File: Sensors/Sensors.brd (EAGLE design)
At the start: 101.6 x 53.3 mm, 36 parts, among them J2 JST_CONNECTOR, J6 JST_CONNECTOR, J7 JST_CONNECTOR, J8 JST_CONNECTOR, J9 JST_CONNECTOR

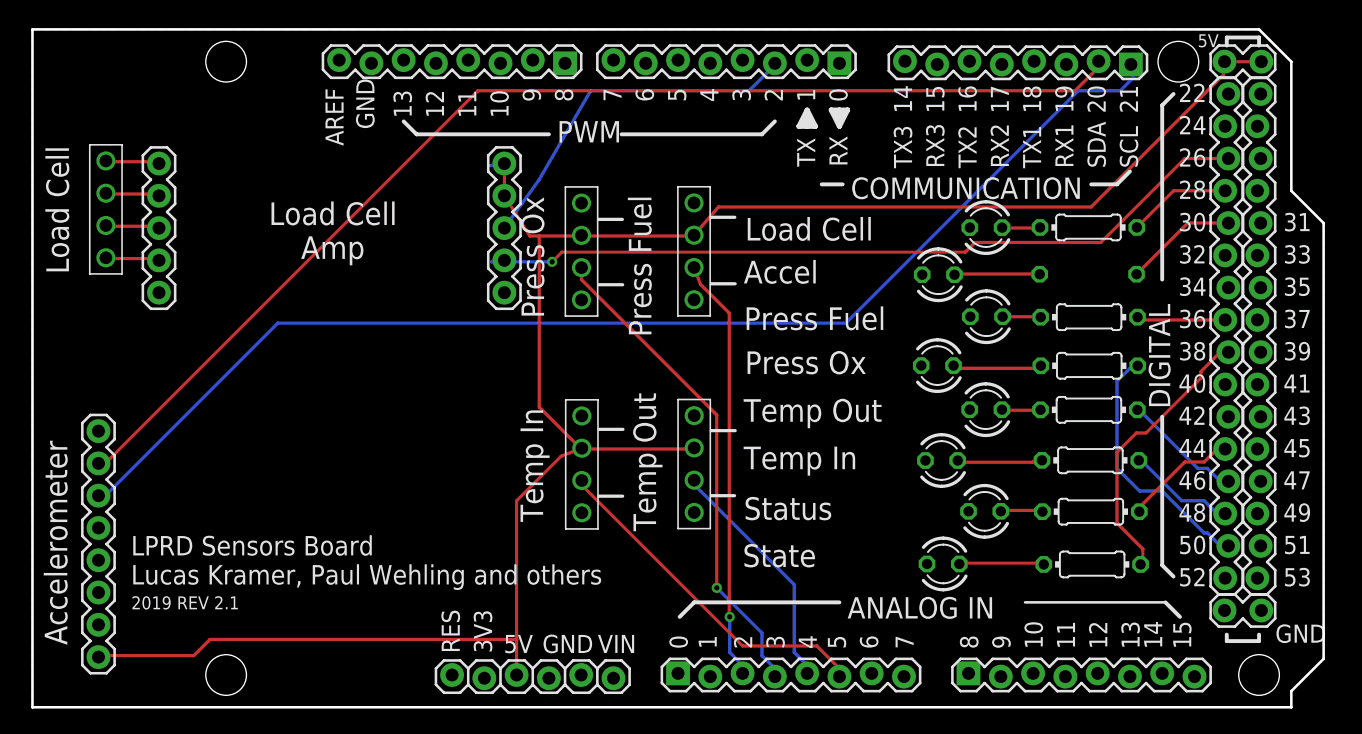
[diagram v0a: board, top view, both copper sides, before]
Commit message: Fix misc. problems found by DRC
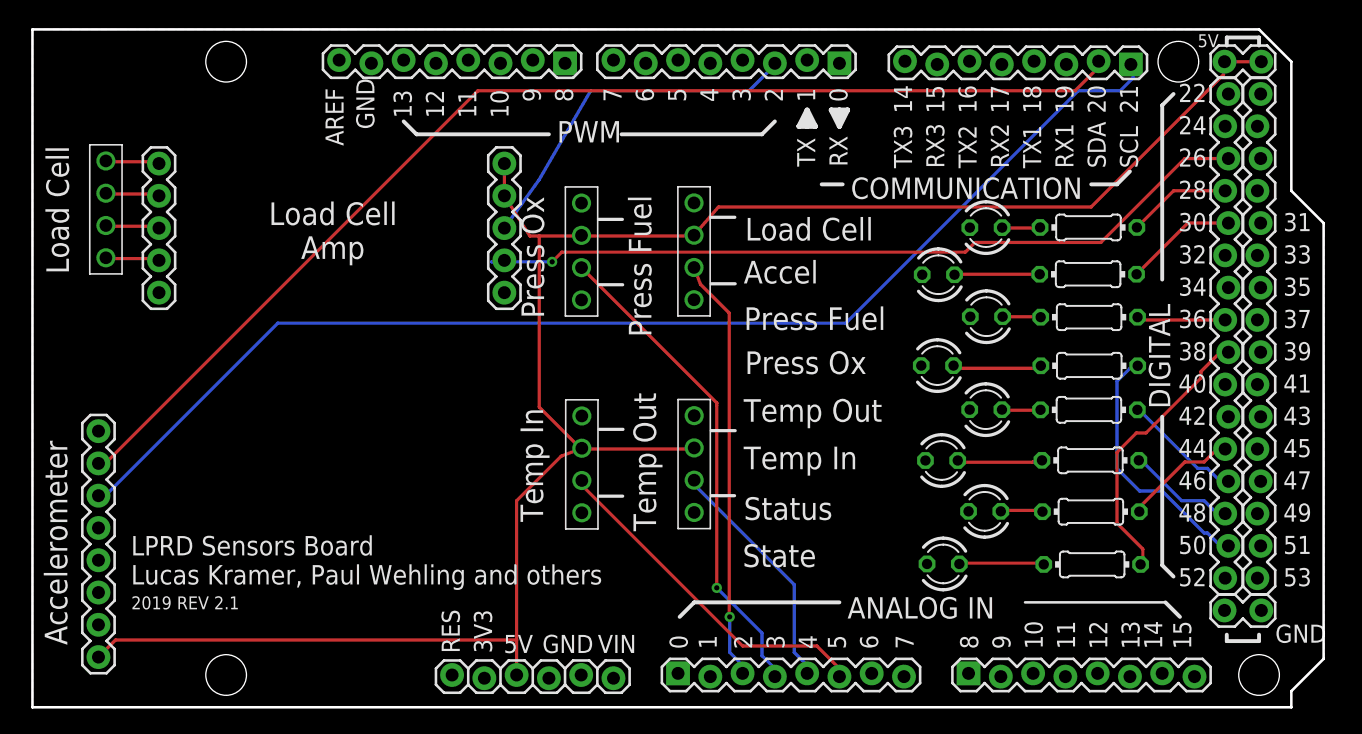
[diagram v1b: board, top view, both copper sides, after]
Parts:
- flipped R1 to the top, turned to 180 degrees
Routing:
- net 5V: track 152.9 -> 151.7 mm
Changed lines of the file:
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@@
 <element name="J9" library="LPRD_RELAY" library_urn="urn:adsk.eagle:library:14231923" package="B4B-XH-A(LF)(SN)" package3d_urn="urn:adsk.eagle:package:14231943/1" value="JST_CONNECTOR" x="43.2054" y="37.1348" smashed="yes" rot="R90"/>
 <element name="J2" library="LPRD_RELAY" library_urn="urn:adsk.eagle:library:14231923" package="B4B-XH-A(LF)(SN)" package3d_urn="urn:adsk.eagle:package:14231943/1" value="JST_CONNECTOR" x="5.7785" y="40.4495" smashed="yes" rot="R90"/>
-<element name="R1" library="rcl" library_urn="urn:adsk.eagle:library:334" package="0204/7" package3d_urn="urn:adsk.eagle:package:23498/2" value="1000" x="83.0707" y="34.0741" smashed="yes" rot="MR0">
-<attribute name="POPULARITY" value="48" x="83.0707" y="34.0741" size="1.778" layer="28" rot="MR0" display="off"/>
-<attribute name="SPICEPREFIX" value="R" x="83.0707" y="34.0741" size="1.778" layer="28" rot="MR0" display="off"/>
+<element name="R1" library="rcl" library_urn="urn:adsk.eagle:library:334" package="0204/7" package3d_urn="urn:adsk.eagle:package:23498/2" value="1000" x="83.0707" y="34.0741" smashed="yes" rot="R180">
+<attribute name="POPULARITY" value="48" x="83.0707" y="34.0741" size="1.778" layer="27" rot="R180" display="off"/>
+<attribute name="SPICEPREFIX" value="R" x="83.0707" y="34.0741" size="1.778" layer="27" rot="R180" display="off"/>
 </element>
 <element name="LED1" library="led" library_urn="urn:adsk.eagle:library:259" package="LED3MM" package3d_urn="urn:adsk.eagle:package:15797/1" value="" x="71.2851" y="34.036" smashed="yes" rot="R180">
@@
 <wire x1="43.3197" y1="20.32" x2="43.2308" y2="20.3835" width="0.254" layer="1"/>
 <wire x1="51.9684" y1="20.32" x2="52.07" y2="20.4089" width="0.254" layer="1"/>
-<wire x1="5.26415" y1="4.00685" x2="5.1943" y2="3.9497" width="0.254" layer="1"/>
 <wire x1="43.0657" y1="37.084" x2="43.2054" y2="37.1348" width="0.254" layer="1"/>
-<wire x1="36.0172" y1="42.6212" x2="37.1348" y2="42.7863" width="0.254" layer="16"/>
 <wire x1="43.0657" y1="37.084" x2="39.878" y2="37.084" width="0.254" layer="1"/>
 <wire x1="39.878" y1="37.084" x2="39.1414" y2="37.084" width="0.254" layer="1"/>
 <wire x1="39.1414" y1="37.084" x2="37.1348" y2="40.2463" width="0.254" layer="1"/>
 <wire x1="37.1348" y1="40.2463" x2="37.1348" y2="42.7863" width="0.254" layer="1"/>
-<wire x1="38.1" y1="16.256" x2="38.1" y2="5.334" width="0.254" layer="1"/>
-<wire x1="38.1" y1="5.334" x2="38.1" y2="2.54" width="0.254" layer="1"/>
+<wire x1="38.1" y1="16.256" x2="38.1" y2="5.2959" width="0.254" layer="1"/>
+<wire x1="38.1" y1="5.2959" x2="38.1" y2="2.54" width="0.254" layer="1"/>
 <wire x1="41.6004375" y1="19.7564375" x2="38.1" y2="16.256" width="0.254" layer="1"/>
 <wire x1="41.6004375" y1="19.7564375" x2="43.2308" y2="20.3835" width="0.254" layer="1"/>
-<wire x1="12.7" y1="4.064" x2="5.334" y2="4.064" width="0.254" layer="1"/>
-<wire x1="13.97" y1="5.334" x2="12.7" y2="4.064" width="0.254" layer="1"/>
-<wire x1="38.1" y1="5.334" x2="13.97" y2="5.334" width="0.254" layer="1"/>
-<wire x1="5.334" y1="4.064" x2="5.1943" y2="3.9497" width="0.254" layer="1"/>
 <wire x1="43.2816" y1="20.2184" x2="43.4213" y2="20.2184" width="0.254" layer="1"/>
 <wire x1="39.878" y1="23.622" x2="43.2816" y2="20.2184" width="0.254" layer="1"/>
 <wire x1="39.878" y1="37.084" x2="39.878" y2="23.622" width="0.254" layer="1"/>
 <wire x1="43.4213" y1="20.2184" x2="43.2308" y2="20.3835" width="0.254" layer="1"/>
+<wire x1="5.1943" y1="3.9497" x2="6.5405" y2="5.2959" width="0.254" layer="1"/>
+<wire x1="6.5405" y1="5.2959" x2="38.1" y2="5.2959" width="0.254" layer="1"/>
 </signal>
 <signal name="GND">
@@
 <contactref element="LED8" pad="K"/>
 <contactref element="LED10" pad="K"/>
-<wire x1="26.67" y1="50.5206" x2="26.67" y2="50.673" width="0.254" layer="16"/>
 <contactref element="J6" pad="P$4"/>
 <contactref element="J7" pad="P$4"/>
@@
 <contactref element="JP7" pad="4"/>
 <contactref element="J9" pad="P$2"/>
-<wire x1="43.2054" y1="34.5948" x2="43.2054" y2="33.6423" width="0.254" layer="1"/>
-<wire x1="53.848" y1="22.9997" x2="43.2054" y2="33.6423" width="0.254" layer="1"/>
-<wire x1="53.848" y1="9.398" x2="53.848" y2="22.9997" width="0.254" layer="1"/>
+<wire x1="53.848" y1="9.398" x2="53.848" y2="23.749" width="0.254" layer="1"/>
+<wire x1="53.848" y1="23.749" x2="53.848" y2="23.9395" width="0.254" layer="1"/>
 <wire x1="57.404" y1="5.842" x2="53.848" y2="9.398" width="0.254" layer="16"/>
 <wire x1="57.404" y1="4.064" x2="57.404" y2="5.842" width="0.254" layer="16"/>
@@
 <wire x1="58.42" y1="2.413" x2="58.42" y2="3.048" width="0.254" layer="16"/>
 <via x="53.848" y="9.398" extent="1-16" drill="0.4064"/>
+<wire x1="43.2054" y1="34.5948" x2="53.848" y2="23.9522" width="0.254" layer="1"/>
+<wire x1="53.848" y1="23.9522" x2="53.848" y2="23.9395" width="0.254" layer="1"/>
 </signal>
 <signal name="VOUT_PRESSURE_OX">
@@
 <contactref element="JP9" pad="12"/>
 <contactref element="R1" pad="1"/>
-<wire x1="94.107" y1="38.1" x2="90.9066" y2="38.1" width="0.254" layer="1"/>
-<wire x1="90.9066" y1="38.1" x2="86.8807" y2="34.0741" width="0.254" layer="1"/>
+<wire x1="86.8807" y1="34.0741" x2="90.9066" y2="38.1" width="0.254" layer="1"/>
+<wire x1="90.9066" y1="38.1" x2="94.107" y2="38.1" width="0.254" layer="1"/>
 </signal>
 <signal name="STATE_LED">
@@
 <contactref element="LED1" pad="A"/>
 <contactref element="R1" pad="2"/>
-<wire x1="72.644" y1="34.0995" x2="72.644" y2="34.036" width="0.254" layer="1"/>
-<wire x1="72.644" y1="34.036" x2="72.5551" y2="34.036" width="0.254" layer="1"/>
-<wire x1="72.644" y1="34.0995" x2="79.2353" y2="34.0995" width="0.254" layer="1"/>
-<wire x1="79.2353" y1="34.0995" x2="79.2607" y2="34.0741" width="0.254" layer="1"/>
+<wire x1="72.5551" y1="34.036" x2="72.5932" y2="34.0741" width="0.254" layer="1"/>
+<wire x1="72.5932" y1="34.0741" x2="79.2607" y2="34.0741" width="0.254" layer="1"/>
 </signal>
 <signal name="D32">

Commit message: Fix backwards pressure pin net names
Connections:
- net VOUT_PRESSURE_FUEL: now also J8.P$2, JP7.3; no longer J9.P$2, JP7.4
- net VOUT_PRESSURE_OX: now also J9.P$2, JP7.4; no longer J8.P$2, JP7.3
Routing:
- net VOUT_PRESSURE_OX: track 33.4 -> 38.5 mm
- net VOUT_PRESSURE_FUEL: track 38.5 -> 33.4 mm
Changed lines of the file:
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@@
 <contactref element="J3" pad="1"/>
 </signal>
-<signal name="VOUT_PRESSURE_FUEL">
+<signal name="VOUT_PRESSURE_OX">
 <contactref element="JP7" pad="4"/>
 <contactref element="J9" pad="P$2"/>
@@
 <wire x1="53.848" y1="23.9522" x2="53.848" y2="23.9395" width="0.254" layer="1"/>
 </signal>
-<signal name="VOUT_PRESSURE_OX">
+<signal name="VOUT_PRESSURE_FUEL">
 <contactref element="JP7" pad="3"/>
 <contactref element="J8" pad="P$2"/>

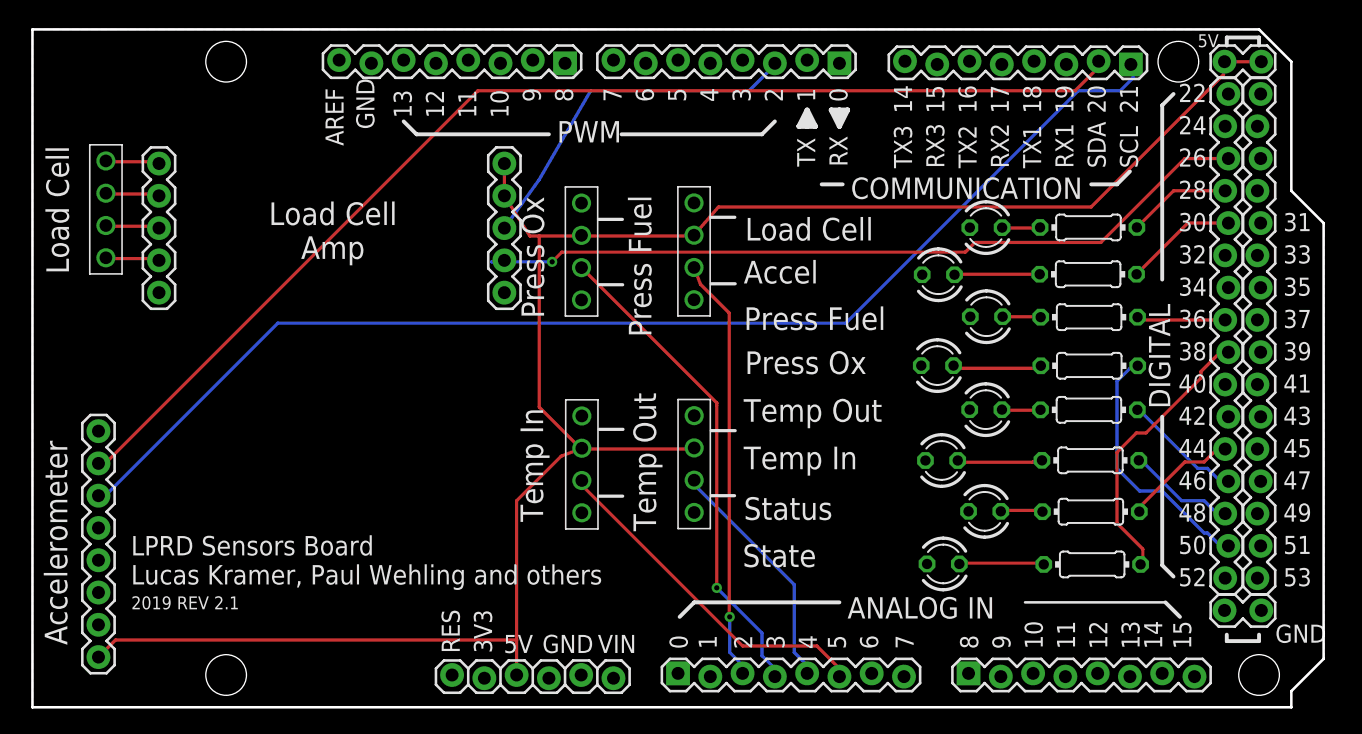
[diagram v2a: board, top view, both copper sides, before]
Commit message: Redesign sensors PCB - remove LEDs and add additional components
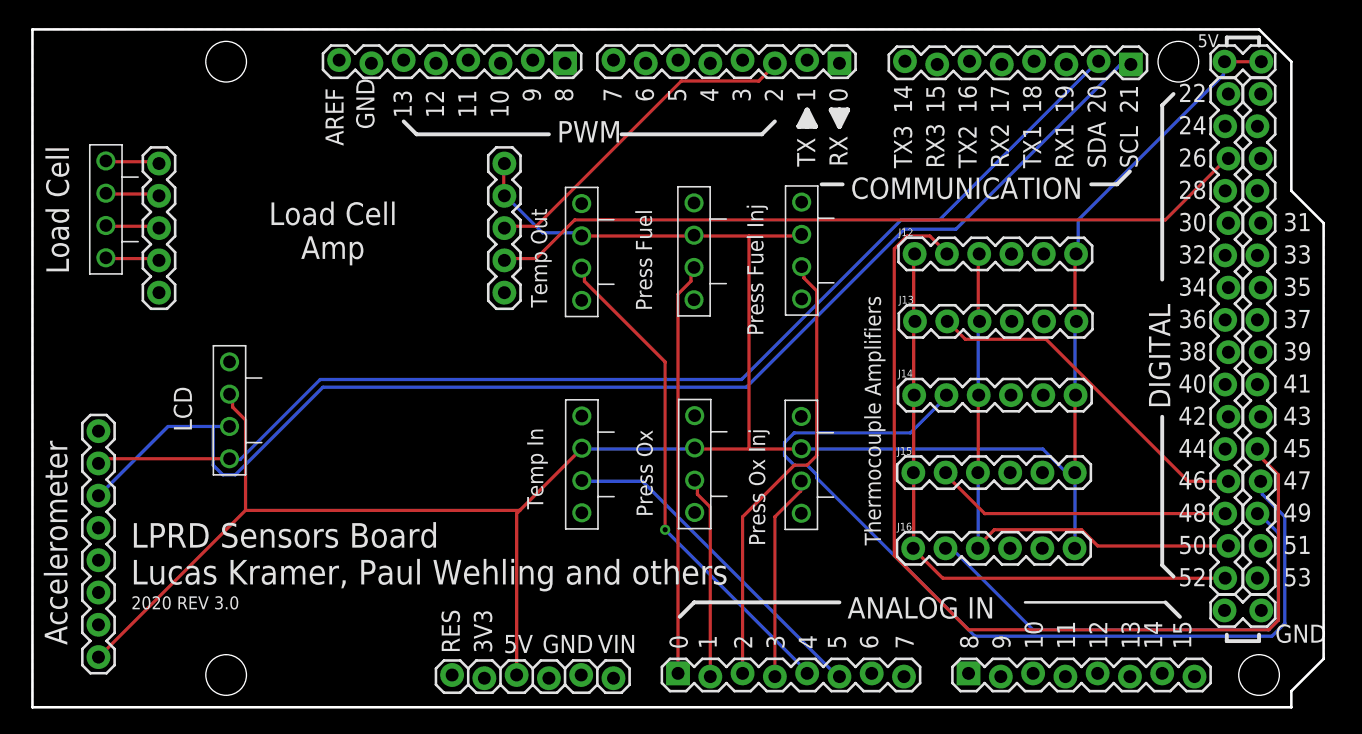
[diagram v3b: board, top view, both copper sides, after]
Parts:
- removed LED1, LED10, LED4, LED5, LED6, LED7, LED8, LED9: (no value), led:LED3MM
- removed R1, R10, R4, R5, R6, R7, R8, R9: 1000, rcl:0204/7
- added J10, J11, J5: JST_CONNECTOR, LPRD_RELAY:B4B-XH-A(LF)(SN)
- added J12, J13, J14, J15, J16: (no value), SparkFun-Connectors:1X06
- moved J9 18.9 mm to (52.1, 20.4)
- moved J6 18.9 mm to (43.2, 37.1)
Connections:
- net D32 renamed VALVE6
- net D34 renamed VALVE8
- net D45 renamed VALVE5
- net D47 renamed VALVE3
- net D49 renamed VALVE1
- net VOUT_TEMPERATURE_IN renamed TEMPERATURE_IN
- net VOUT_TEMPERATURE_OUT renamed TEMPERATURE_OUT
- removed net A0: JP7.1
- removed net A1: JP7.2
- removed net ACCEL_LED: JP9.12, R1.1
- removed net D27: JP8.3
- removed net D29: JP8.4
- removed net D31: JP8.5
- removed net D33: JP8.6
- removed net D52: JP9.1
- removed net FORCE_LED: JP9.13, R4.1
- removed net N$1: LED1.A, R1.2
- removed net N$15: LED8.A, R8.2
- removed net N$16: LED9.A, R9.2
- removed net N$23: LED10.A, R10.2
- removed net N$4: LED4.A, R4.2
- removed net N$5: LED5.A, R5.2
- removed net N$6: LED6.A, R6.2
- removed net N$7: LED7.A, R7.2
- removed net PRESSURE_FUEL_LED: JP9.9, R5.1
- removed net PRESSURE_OX_LED: JP9.2, R10.1
- removed net STATE_LED: JP9.8, R6.1
- removed net STATUS_LED: JP9.5, R7.1
- removed net TEMP_IN_LED: JP9.3, R9.1
- removed net TEMP_OUT_LED: JP9.4, R8.1
- removed net VOUT_PRESSURE_FUEL: J8.P$2, JP7.3
- removed net VOUT_PRESSURE_OX: J9.P$2, JP7.4
- new net D14: JP5.8
- new net D36: JP9.9
- new net D38: JP9.8
- new net D44: JP9.5
- new net IGNITION: JP5.7
- new net MISO: J12.3, J13.3, J14.3, J15.3, J16.3, JP9.2
- new net PRESSURE_FUEL: J8.P$2, JP7.1
- new net PRESSURE_FUEL_INJ: J5.P$2, JP7.3
- new net PRESSURE_OX: J9.P$2, JP7.2
- new net PRESSURE_OX_INJ: J10.P$2, JP7.4
- new net SCK: J12.1, J13.1, J14.1, J15.1, J16.1, JP9.1
- new net THERMO_CS1: J12.2, JP8.5
- new net THERMO_CS2: J13.2, JP9.4
- new net THERMO_CS3: J14.2, JP8.4
- new net THERMO_CS4: J15.2, JP9.3
- new net THERMO_CS5: J16.2, JP8.3
- new net VALVE2: JP9.13
- new net VALVE4: JP9.12
- new net VALVE7: JP8.11
- net 5V: now also J10.P$3, J11.P$3, J12.6, J13.6, J14.6, J15.6, J16.6, J5.P$3
- net D23: now also JP8.16; no longer JP8.1
- net D25: now also JP8.15; no longer JP8.2
- net D35: now also JP8.10; no longer JP8.7
- net D37: now also JP8.9; no longer JP8.8
- net D39: now also JP8.8; no longer JP8.9
- net D41: now also JP8.7; no longer JP8.10
- net D43: now also JP8.6; no longer JP8.11
- net D51: now also JP8.2; no longer JP8.15
- net D53: now also JP8.1; no longer JP8.16
- net GND: now also J10.P$4, J11.P$4, J12.4, J13.4, J14.4, J15.4, J16.4, J5.P$4; no longer LED1.K, LED10.K, LED4.K, LED5.K, LED6.K, LED7.K, LED8.K, LED9.K
- net SCL: now also J11.P$2
- net SDA: now also J11.P$1
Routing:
- net THERMO_CS1: track 0.00 -> 76.5 mm
- net THERMO_CS3: track 0.00 -> 73.2 mm
- net SCK: track 0.00 -> 48.8 mm
- net 5V: track 151.7 -> 197.8 mm
- net MISO: track 0.00 -> 44.2 mm
- net VOUT_PRESSURE_OX: track 38.5 -> 0.00 mm, vias 1 -> 0
- net THERMO_CS5: track 0.00 -> 38.3 mm
- net PRESSURE_FUEL_INJ: track 0.00 -> 35.5 mm
- net VOUT_PRESSURE_FUEL: track 33.4 -> 0.00 mm, vias 1 -> 0
- net PRESSURE_FUEL: track 0.00 -> 32.5 mm
- net THERMO_CS2: track 0.00 -> 27.3 mm
- net THERMO_CS4: track 0.00 -> 23.4 mm
- net STATE_LED: track 22.1 -> 0.00 mm
- net PRESSURE_OX_LED: track 20.3 -> 0.00 mm
- net TEMPERATURE_OUT: track 19.2 -> 39.4 mm, vias 0 -> 1
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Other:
- board text added: "2020 REV 3.0"
- board text added: "LCD"
- board text added: "Press Fuel Inj"
- board text added: "Press Ox Inj"
- board text added: "Thermocouple Amplifiers"
- board text removed: "2019 REV 2.1"
- board text removed: "Accel"
- board text removed: "State"
- board text removed: "Status"

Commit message: Change header package to remove staggered pins
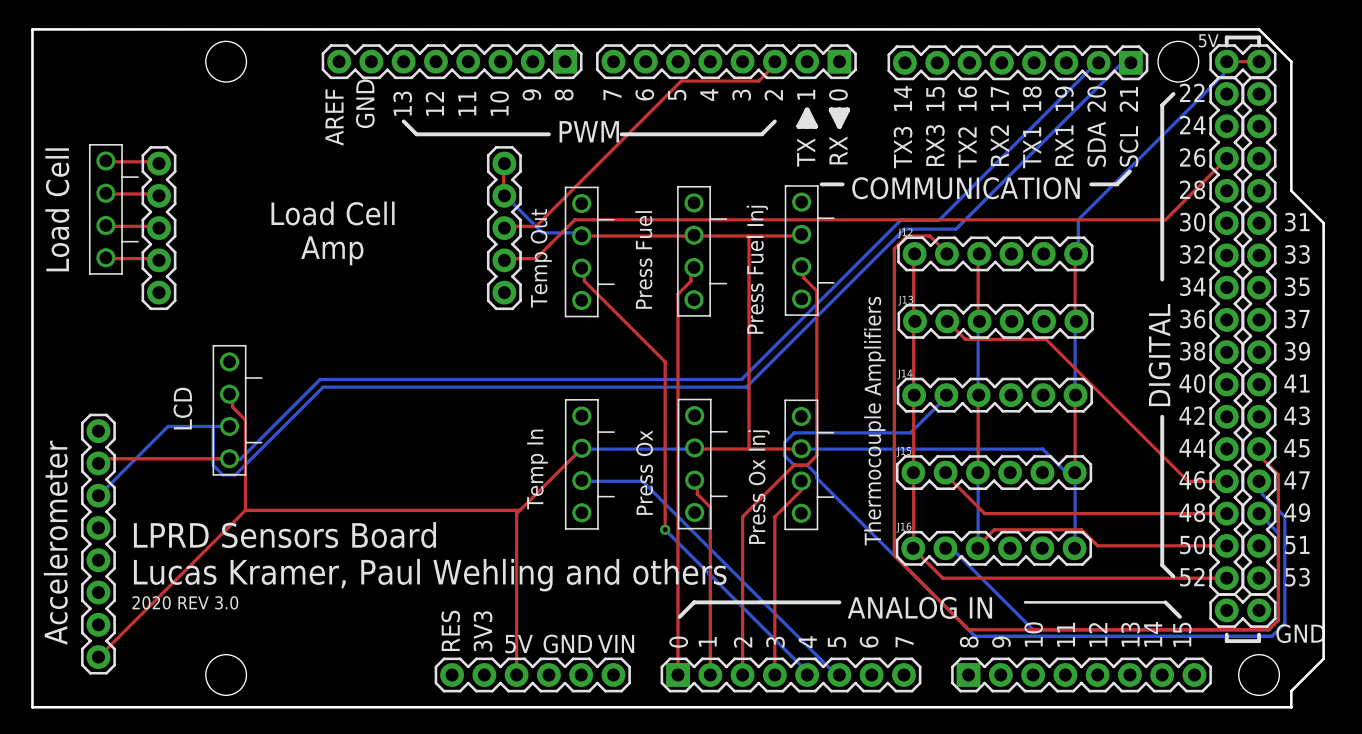
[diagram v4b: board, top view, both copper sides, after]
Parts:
- JP10: device SparkFun:1X06_LOCK -> SparkFun:1X06
- JP11, JP12: device SparkFun:1X02_LOCK -> SparkFun:1X02
- JP3, JP4, JP5, JP6, JP7: device SparkFun:1X08_LOCK -> SparkFun:1X08
- JP8, JP9: value M16LOCK -> M16PTH; device SparkFun:1X16_LOCK -> SparkFun:1X16
